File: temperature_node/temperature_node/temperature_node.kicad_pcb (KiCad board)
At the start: 4 copper layers, 23 x 24.5 mm, 35 parts, among them CN1 UART, J1 USB_C_Receptacle_USB2.0_16P, J2 S2B-PH-K-S, J3 IO9, U1 SHT40-AD1B-R3, U2 MCP73831-2-OT, U3 MIC5504-3.3YM5, U4 ESP32-C3-WROOM-02, U6 USBLC6-2P6

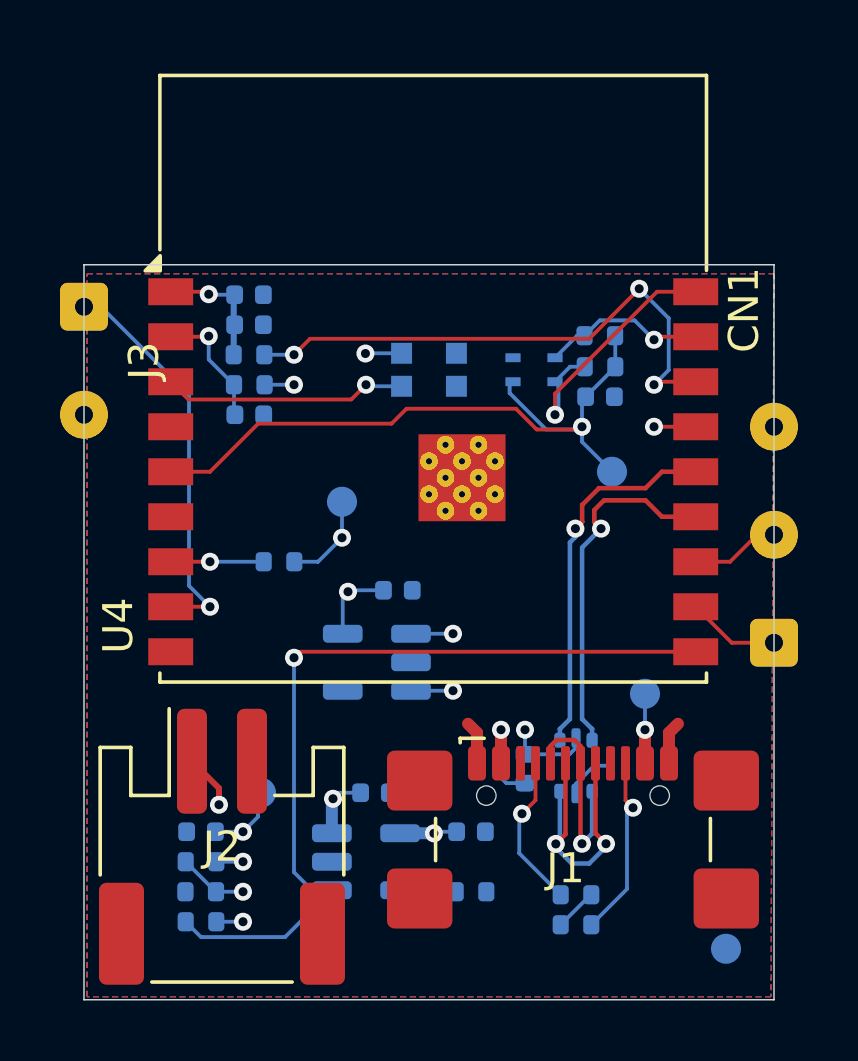
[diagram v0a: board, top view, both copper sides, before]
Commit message: Remove some DRC warnings
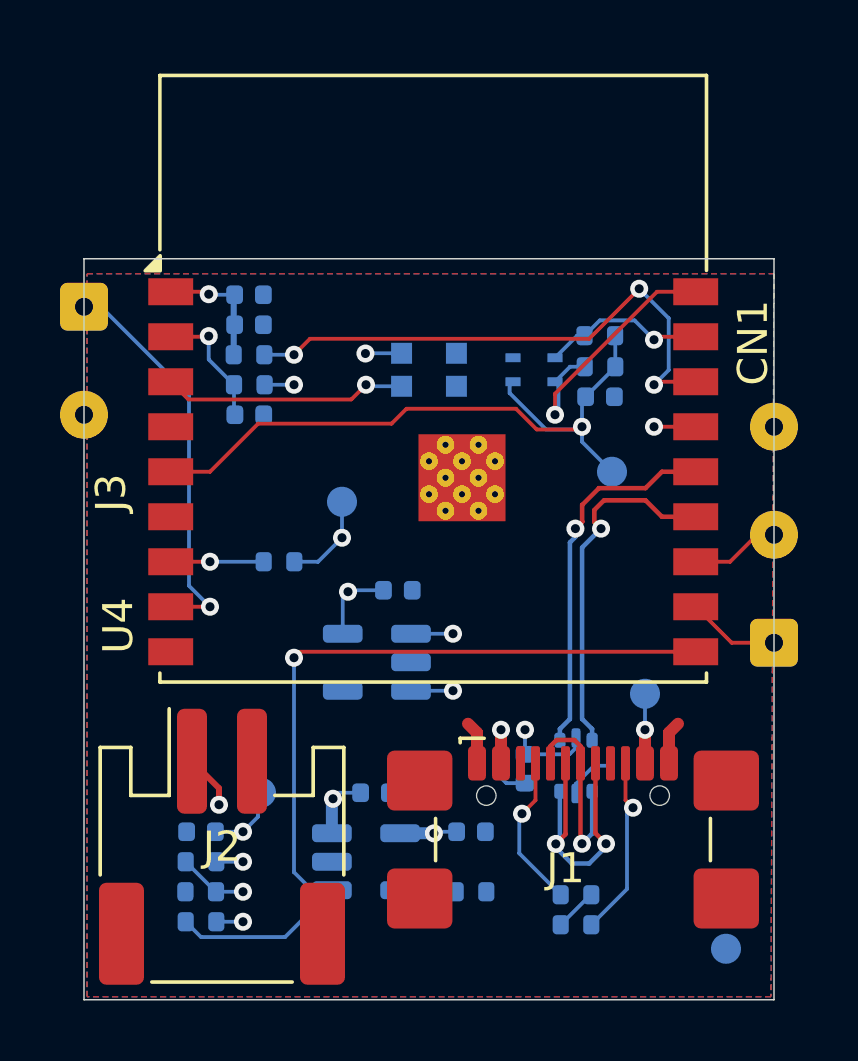
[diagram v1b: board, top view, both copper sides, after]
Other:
- board size 23 x 24.5 mm -> 23 x 24.7 mm
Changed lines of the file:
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@@
 		(tags "connector wire 0.1sqmm")
 		(property "Reference" "J3"
-			(at 1.8 -2 90)
+			(at 6.2 -0.9 90)
 			(layer "F.SilkS")
 			(effects
@@
 		)
 		(fp_text user "${REFERENCE}"
-			(at 1.8 0 360)
+			(at 1.8 0 0)
 			(layer "F.Fab")
 			(effects
@@
 		(tags "connector wire 0.1sqmm")
 		(property "Reference" "CN1"
-			(at 11.09 -1 90)
+			(at 10 -0.7 90)
 			(layer "F.SilkS")
 			(effects
@@
 		(tags "resistor")
 		(property "Reference" "R3"
-			(at 0 1.17 360)
+			(at 0 1.17 0)
 			(layer "B.SilkS")
 			(effects
@@
 		)
 		(property "Value" "10k"
-			(at 0 -1.17 360)
+			(at 0 -1.17 0)
 			(layer "B.Fab")
 			(effects
@@
 		)
 		(fp_text user "${REFERENCE}"
-			(at 0 0 360)
+			(at 0 0 0)
 			(layer "B.Fab")
 			(effects
@@
 		(tags "resistor")
 		(property "Reference" "R11"
-			(at 2.5 0 360)
+			(at 2.5 0 0)
 			(layer "B.SilkS")
 			(effects
@@
 		)
 		(property "Value" "100k"
-			(at 0 -1.17 360)
+			(at 0 -1.17 0)
 			(layer "B.Fab")
 			(effects
@@
 		)
 		(fp_text user "${REFERENCE}"
-			(at 0 0 360)
+			(at 0 0 0)
 			(layer "B.Fab")
 			(effects
@@
 		(tags "SOT TO_SOT_SMD")
 		(property "Reference" "U2"
-			(at 0 2.4 360)
+			(at 0 2.4 0)
 			(layer "B.SilkS")
 			(effects
@@
 		)
 		(property "Value" "MCP73831-2-OT"
-			(at 0 -2.4 360)
+			(at 0 -2.4 0)
 			(layer "B.Fab")
 			(effects
@@
 		)
 		(fp_text user "${REFERENCE}"
-			(at 0 0 360)
+			(at 0 0 0)
 			(layer "B.Fab")
 			(effects
@@
 		(tags "capacitor")
 		(property "Reference" "C2"
-			(at 2.5 0.5 360)
+			(at 2.5 0.5 0)
 			(layer "B.SilkS")
 			(effects
@@
 		)
 		(property "Value" "4u7"
-			(at 0 -1 360)
+			(at 0 -1 0)
 			(layer "B.Fab")
 			(effects
@@
 		)
 		(fp_text user "${REFERENCE}"
-			(at 0 0 360)
+			(at 0 0 0)
 			(layer "B.Fab")
 			(effects
@@
 		(tags "capacitor")
 		(property "Reference" "C5"
-			(at -0.049122 1.202403 360)
+			(at -0.049122 1.202403 0)
 			(layer "B.SilkS")
 			(effects
@@
 		)
 		(property "Value" "1u"
-			(at 0 -1.16 360)
+			(at 0 -1.16 0)
 			(layer "B.Fab")
 			(effects
@@
 		)
 		(fp_text user "${REFERENCE}"
-			(at 0 0 360)
+			(at 0 0 0)
 			(layer "B.Fab")
 			(effects
@@
 		(tags "resistor")
 		(property "Reference" "R12"
-			(at 2.49 -0.5 360)
+			(at 2.49 -0.5 0)
 			(layer "B.SilkS")
 			(effects
@@
 		)
 		(property "Value" "100k"
-			(at 0 -1.17 360)
+			(at 0 -1.17 0)
 			(layer "B.Fab")
 			(effects
@@
 		)
 		(fp_text user "${REFERENCE}"
-			(at 0 0 360)
+			(at 0 0 0)
 			(layer "B.Fab")
 			(effects
@@
 		)
 		(fp_text user "${REFERENCE}"
-			(at 0 0 360)
+			(at 0 0 0)
 			(layer "B.Fab")
 			(effects
@@
 		(tags "capacitor")
 		(property "Reference" "C3"
-			(at 3 0.5 360)
+			(at 3 0.5 0)
 			(layer "B.SilkS")
 			(effects
@@
 		)
 		(property "Value" "4u7"
-			(at 0 -1.5 360)
+			(at 0 -1.5 0)
 			(layer "B.Fab")
 			(effects
@@
 		)
 		(fp_text user "${REFERENCE}"
-			(at 0 0 360)
+			(at 0 0 0)
 			(layer "B.Fab")
 			(effects
@@
 		)
 		(property "Value" "1u"
-			(at 0 -1.16 360)
+			(at 0 -1.16 0)
 			(layer "B.Fab")
 			(effects
@@
 		)
 		(fp_text user "${REFERENCE}"
-			(at 0 0 360)
+			(at 0 0 0)
 			(layer "B.Fab")
 			(effects
@@
 		(tags "resistor")
 		(property "Reference" "R4"
-			(at 2 0 360)
+			(at 2 0 0)
 			(layer "B.SilkS")
 			(effects
@@
 		)
 		(property "Value" "10k"
-			(at 0 -1.17 360)
+			(at 0 -1.17 0)
 			(layer "B.Fab")
 			(effects
@@
 		)
 		(fp_text user "${REFERENCE}"
-			(at 0 0 360)
+			(at 0 0 0)
 			(layer "B.Fab")
 			(effects
@@
 	)
 	(gr_rect
-		(start 121 80)
+		(start 121 79.8)
 		(end 144 104.5)
 		(stroke

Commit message: Constellation pads added property for DRC
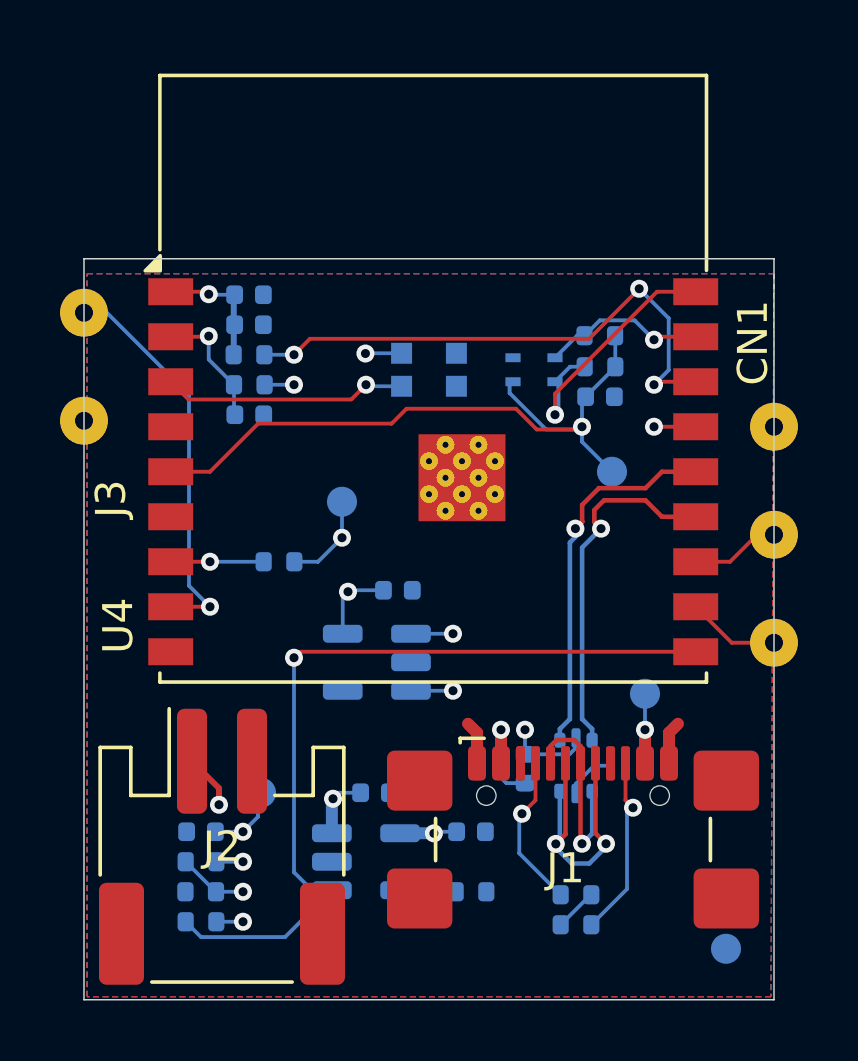
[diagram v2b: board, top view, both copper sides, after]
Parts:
- moved J3 0.20 mm to (121.0, 81.6)
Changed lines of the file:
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@@
 	(footprint "Connector_Wire:SolderWire-0.1sqmm_1x02_P3.6mm_D0.4mm_OD1mm"
 		(layer "F.Cu")
-		(at 121 81.4 -90)
+		(at 121 81.6 -90)
 		(descr "Soldered wire connection, for 2 times 0.1 mm² wires, basic insulation, conductor diameter 0.4mm, outer diameter 1mm, size source Multi-Contact FLEXI-E 0.1 (https://ec.staubli.com/AcroFiles/Catalogues/TM_Cab-Main-11014119_(en)_hi.pdf), bend radius 3 times outer diameter, generated with kicad-footprint-generator")
 		(tags "connector wire 0.1sqmm")
@@
 			)
 		)
-		(pad "1" thru_hole roundrect
+		(pad "1" thru_hole circle
 			(at 0 0 270)
 			(size 1.6 1.6)
 			(drill 0.6)
+			(property pad_prop_castellated)
 			(layers "*.Cu" "*.Mask")
 			(remove_unused_layers no)
-			(roundrect_rratio 0.15625)
 			(net 20 "Net-(J3-Pin_1)")
 			(pinfunction "Pin_1")
@@
 			(size 1.6 1.6)
 			(drill 0.6)
+			(property pad_prop_castellated)
 			(layers "*.Cu" "*.Mask")
 			(remove_unused_layers no)
@@
 			)
 		)
-		(pad "1" thru_hole roundrect
+		(pad "1" thru_hole circle
 			(at 0 0 90)
 			(size 1.6 1.6)
 			(drill 0.6)
+			(property pad_prop_castellated)
 			(layers "*.Cu" "*.Mask")
 			(remove_unused_layers no)
-			(roundrect_rratio 0.15625)
 			(net 8 "/RX")
 			(pinfunction "Pin_1")
@@
 			(size 1.6 1.6)
 			(drill 0.6)
+			(property pad_prop_castellated)
 			(layers "*.Cu" "*.Mask")
 			(remove_unused_layers no)
@@
 			(size 1.6 1.6)
 			(drill 0.6)
+			(property pad_prop_castellated)
 			(layers "*.Cu" "*.Mask")
 			(remove_unused_layers no)

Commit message: Apply sch changes
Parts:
- removed CN1: UART, Connector_Wire:SolderWire-0.1sqmm_1x03_P3.6mm_D0.4mm_OD1mm
- removed J3: IO9, Connector_Wire:SolderWire-0.1sqmm_1x02_P3.6mm_D0.4mm_OD1mm
- added TP6: RX, TestPoint:TestPoint_Pad_D1.0mm, B.Cu at (141.9, 88.0)
- added TP7: TX, TestPoint:TestPoint_Pad_D1.0mm, B.Cu at (141.9, 91.0)
- added TP8: IO9, TestPoint:TestPoint_Pad_D1.0mm, B.Cu at (141.9, 94.1)
- moved TP1 3.64 mm to (141.9, 97.2)
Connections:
- U4 pad 8: Net-(J3-Pin_1) -> /IO9
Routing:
- net /IO9: track 0.00 -> 19.1 mm, vias 0 -> 1
- net Net-(J3-Pin_1): track 12.8 -> 0.00 mm, vias 1 -> 0
- net /RX: track 2.54 -> 9.70 mm, vias 0 -> 1
- net /TX: track 2.42 -> 6.59 mm, vias 0 -> 1
- net VBUS: track 8.28 -> 9.99 mm

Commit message: PCB DRC Ok
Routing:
- net GND: track 7.01 -> 23.9 mm, vias 0 -> 23
- net /RX: track 9.70 -> 7.15 mm
- net /TX: track 6.59 -> 4.17 mm
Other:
- board size 23 x 24.7 mm -> 23 x 31.3 mm

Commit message: Reanotate PCB and SCH
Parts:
- renumbered C6 to C2, C8 to C3, C7 to C4, C3 to C6, C4 to C7, C9 to C8, C2 to C9, D3 to D1, R2 to R1, R4 to R10, R9 to R11, R10 to R2, R8 to R3, R1 to R4, R3 to R5, R5 to R6, R11 to R7, R12 to R8, R6 to R9, TP6 to TP1, TP4 to TP2, TP7 to TP4, TP1 to TP6, TP8 to TP7, TP2 to TP8, U4 to U1, U1 to U2, U2 to U3, U6 to U4, U3 to U5
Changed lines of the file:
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@@
 		(descr "RF Module, ESP32-C3 WROOM-02, Wi-Fi and Bluetooth, BLE, onboard antenna, https://www.espressif.com/sites/default/files/documentation/esp32-c3-wroom-02_datasheet_en.pdf")
 		(tags "ESP32-C3 WROOM-02 espressif")
-		(property "Reference" "U4"
+		(property "Reference" "U1"
 			(at -10.5 5.13 90)
 			(layer "F.SilkS")
@@
 		(descr "Resistor SMD 0402 (1005 Metric), square (rectangular) end terminal, IPC_7351 nominal, (Body size source: IPC-SM-782 page 72, https://www.pcb-3d.com/wordpress/wp-content/uploads/ipc-sm-782a_amendment_1_and_2.pdf), generated with kicad-footprint-generator")
 		(tags "resistor")
-		(property "Reference" "R3"
+		(property "Reference" "R5"
 			(at 0 1.17 0)
 			(layer "B.SilkS")
@@
 		(descr "Resistor SMD 0402 (1005 Metric), square (rectangular) end terminal, IPC_7351 nominal, (Body size source: IPC-SM-782 page 72, https://www.pcb-3d.com/wordpress/wp-content/uploads/ipc-sm-782a_amendment_1_and_2.pdf), generated with kicad-footprint-generator")
 		(tags "resistor")
-		(property "Reference" "R5"
+		(property "Reference" "R6"
 			(at -2.5 0 0)
 			(layer "B.SilkS")
@@
 		(descr "Sensirion, SHT40, SHT41, SHT45, DFN, 4 Pin (https://sensirion.com/media/documents/33FD6951/624C4357/Datasheet_SHT4x.pdf)")
 		(tags "DFN NoLead")
-		(property "Reference" "U1"
+		(property "Reference" "U2"
 			(at 0.2 -2 0)
 			(layer "B.SilkS")
@@
 		(descr "Resistor SMD 0402 (1005 Metric), square (rectangular) end terminal, IPC_7351 nominal, (Body size source: IPC-SM-782 page 72, https://www.pcb-3d.com/wordpress/wp-content/uploads/ipc-sm-782a_amendment_1_and_2.pdf), generated with kicad-footprint-generator")
 		(tags "resistor")
-		(property "Reference" "R11"
+		(property "Reference" "R7"
 			(at 2.5 0 0)
 			(layer "B.SilkS")
@@
 		(descr "Capacitor SMD 0402 (1005 Metric), square (rectangular) end terminal, IPC_7351 nominal, (Body size source: IPC-SM-782 page 76, https://www.pcb-3d.com/wordpress/wp-content/uploads/ipc-sm-782a_amendment_1_and_2.pdf), generated with kicad-footprint-generator")
 		(tags "capacitor")
-		(property "Reference" "C7"
+		(property "Reference" "C4"
 			(at -2.5 0 0)
 			(layer "B.SilkS")
@@
 		(descr "Resistor SMD 0402 (1005 Metric), square (rectangular) end terminal, IPC_7351 nominal, (Body size source: IPC-SM-782 page 72, https://www.pcb-3d.com/wordpress/wp-content/uploads/ipc-sm-782a_amendment_1_and_2.pdf), generated with kicad-footprint-generator")
 		(tags "resistor")
-		(property "Reference" "R8"
+		(property "Reference" "R3"
 			(at -2.298321 -1.073385 0)
 			(layer "B.SilkS")
@@
 		(descr "SMD pad as test Point, diameter 1.0mm")
 		(tags "test point SMD pad")
-		(property "Reference" "TP1"
+		(property "Reference" "TP6"
 			(at 0 -1.9 0)
 			(layer "B.SilkS")
@@
 		(descr "SMD pad as test Point, diameter 1.0mm")
 		(tags "test point SMD pad")
-		(property "Reference" "TP6"
+		(property "Reference" "TP1"
 			(at 0 1.448 0)
 			(layer "B.SilkS")
@@
 		(descr "SOT, 5 Pin (https://www.jedec.org/sites/default/files/docs/Mo-178c.PDF variant AA), generated with kicad-footprint-generator ipc_gullwing_generator.py")
 		(tags "SOT TO_SOT_SMD")
-		(property "Reference" "U2"
+		(property "Reference" "U3"
 			(at 0 2.4 0)
 			(layer "B.SilkS")
@@
 		(descr "SMD pad as test Point, diameter 1.0mm")
 		(tags "test point SMD pad")
-		(property "Reference" "TP2"
+		(property "Reference" "TP8"
 			(at 2.5 0 0)
 			(layer "B.SilkS")
@@
 		(descr "Capacitor SMD 0402 (1005 Metric), square (rectangular) end terminal, IPC_7351 nominal, (Body size source: IPC-SM-782 page 76, https://www.pcb-3d.com/wordpress/wp-content/uploads/ipc-sm-782a_amendment_1_and_2.pdf), generated with kicad-footprint-generator")
 		(tags "capacitor")
-		(property "Reference" "C6"
+		(property "Reference" "C2"
 			(at -2.5 1.5 0)
 			(layer "B.SilkS")
@@
 		(descr "Capacitor SMD 0402 (1005 Metric), square (rectangular) end terminal, IPC_7351 nominal, (Body size source: IPC-SM-782 page 76, https://www.pcb-3d.com/wordpress/wp-content/uploads/ipc-sm-782a_amendment_1_and_2.pdf), generated with kicad-footprint-generator")
 		(tags "capacitor")
-		(property "Reference" "C8"
+		(property "Reference" "C3"
 			(at -2.5 0.5 0)
 			(layer "B.SilkS")
@@
 		(descr "Resistor SMD 0402 (1005 Metric), square (rectangular) end terminal, IPC_7351 nominal, (Body size source: IPC-SM-782 page 72, https://www.pcb-3d.com/wordpress/wp-content/uploads/ipc-sm-782a_amendment_1_and_2.pdf), generated with kicad-footprint-generator")
 		(tags "resistor")
-		(property "Reference" "R2"
+		(property "Reference" "R1"
 			(at -2.307825 0.365343 0)
 			(layer "B.SilkS")
@@
 		(descr "SMD pad as test Point, diameter 1.0mm")
 		(tags "test point SMD pad")
-		(property "Reference" "TP7"
+		(property "Reference" "TP4"
 			(at 0 1.448 0)
 			(layer "B.SilkS")
@@
 		(descr "Resistor SMD 0402 (1005 Metric), square (rectangular) end terminal, IPC_7351 nominal, (Body size source: IPC-SM-782 page 72, https://www.pcb-3d.com/wordpress/wp-content/uploads/ipc-sm-782a_amendment_1_and_2.pdf), generated with kicad-footprint-generator")
 		(tags "resistor")
-		(property "Reference" "R6"
+		(property "Reference" "R9"
 			(at 0 1.2 0)
 			(layer "B.SilkS")
@@
 		(descr "SMD pad as test Point, diameter 1.0mm")
 		(tags "test point SMD pad")
-		(property "Reference" "TP4"
+		(property "Reference" "TP2"
 			(at 2.5 0 0)
 			(layer "B.SilkS")
@@
 		(descr "Capacitor SMD 0402 (1005 Metric), square (rectangular) end terminal, IPC_7351 nominal, (Body size source: IPC-SM-782 page 76, https://www.pcb-3d.com/wordpress/wp-content/uploads/ipc-sm-782a_amendment_1_and_2.pdf), generated with kicad-footprint-generator")
 		(tags "capacitor")
-		(property "Reference" "C9"
+		(property "Reference" "C8"
 			(at -0.6 1.16 90)
 			(layer "B.SilkS")
@@
 		(descr "Capacitor SMD 0402 (1005 Metric), square (rectangular) end terminal, IPC_7351 nominal, (Body size source: IPC-SM-782 page 76, https://www.pcb-3d.com/wordpress/wp-content/uploads/ipc-sm-782a_amendment_1_and_2.pdf), generated with kicad-footprint-generator")
 		(tags "capacitor")
-		(property "Reference" "C2"
+		(property "Reference" "C9"
 			(at 2.5 0.5 0)
 			(layer "B.SilkS")
@@
 		(descr "Resistor SMD 0402 (1005 Metric), square (rectangular) end terminal, IPC_7351 nominal, (Body size source: IPC-SM-782 page 72, https://www.pcb-3d.com/wordpress/wp-content/uploads/ipc-sm-782a_amendment_1_and_2.pdf), generated with kicad-footprint-generator")
 		(tags "resistor")
-		(property "Reference" "R12"
+		(property "Reference" "R8"
 			(at 2.49 -0.4 0)
 			(layer "B.SilkS")
@@
 		(descr "SOT666")
 		(tags "SOT-666")
-		(property "Reference" "U6"
+		(property "Reference" "U4"
 			(at 2.4 0 180)
 			(layer "B.SilkS")
@@
 		(descr "Capacitor SMD 0402 (1005 Metric), square (rectangular) end terminal, IPC_7351 nominal, (Body size source: IPC-SM-782 page 76, https://www.pcb-3d.com/wordpress/wp-content/uploads/ipc-sm-782a_amendment_1_and_2.pdf), generated with kicad-footprint-generator")
 		(tags "capacitor")
-		(property "Reference" "C3"
+		(property "Reference" "C6"
 			(at 3 0.5 0)
 			(layer "B.SilkS")
@@
 		(descr "Capacitor SMD 0402 (1005 Metric), square (rectangular) end terminal, IPC_7351 nominal, (Body size source: IPC-SM-782 page 76, https://www.pcb-3d.com/wordpress/wp-content/uploads/ipc-sm-782a_amendment_1_and_2.pdf), generated with kicad-footprint-generator")
 		(tags "capacitor")
-		(property "Reference" "C4"
+		(property "Reference" "C7"
 			(at 2 0 90)
 			(layer "B.SilkS")
@@
 		(descr "Resistor SMD 0402 (1005 Metric), square (rectangular) end terminal, IPC_7351 nominal, (Body size source: IPC-SM-782 page 72, https://www.pcb-3d.com/wordpress/wp-content/uploads/ipc-sm-782a_amendment_1_and_2.pdf), generated with kicad-footprint-generator")
 		(tags "resistor")
-		(property "Reference" "R1"
+		(property "Reference" "R4"
 			(at -2.3 -0.1 0)
 			(layer "B.SilkS")
@@
 		(descr "SOT, 5 Pin (https://www.jedec.org/sites/default/files/docs/Mo-178c.PDF variant AA), generated with kicad-footprint-generator ipc_gullwing_generator.py")
 		(tags "SOT TO_SOT_SMD")
-		(property "Reference" "U3"
+		(property "Reference" "U5"
 			(at 3.1375 -2.05 0)
 			(layer "B.SilkS")
@@
 		(descr "Resistor SMD 0402 (1005 Metric), square (rectangular) end terminal, IPC_7351 nominal, (Body size source: IPC-SM-782 page 72, https://www.pcb-3d.com/wordpress/wp-content/uploads/ipc-sm-782a_amendment_1_and_2.pdf), generated with kicad-footprint-generator")
 		(tags "resistor")
-		(property "Reference" "R4"
+		(property "Reference" "R10"
 			(at 2 -0.8 0)
 			(layer "B.SilkS")
@@
 		(descr "SMD pad as test Point, diameter 1.0mm")
 		(tags "test point SMD pad")
-		(property "Reference" "TP8"
+		(property "Reference" "TP7"
 			(at 0 1.448 0)
 			(layer "B.SilkS")
@@
 		(descr "Resistor SMD 0402 (1005 Metric), square (rectangular) end terminal, IPC_7351 nominal, (Body size source: IPC-SM-782 page 72, https://www.pcb-3d.com/wordpress/wp-content/uploads/ipc-sm-782a_amendment_1_and_2.pdf), generated with kicad-footprint-generator")
 		(tags "resistor")
-		(property "Reference" "R9"
+		(property "Reference" "R11"
 			(at -2.5 0 0)
 			(layer "B.SilkS")
@@
 		(descr "2.0mm x 2.0mm Addressable RGB LED NeoPixel Nano, 12 mA, https://cdn-shop.adafruit.com/product-files/4684/4684_WS2812B-2020_V1.3_EN.pdf")
 		(tags "LED RGB NeoPixel Nano PLCC-4 2020")
-		(property "Reference" "D3"
+		(property "Reference" "D1"
 			(at 0 2 0)
 			(layer "B.SilkS")
@@
 		(descr "Resistor SMD 0402 (1005 Metric), square (rectangular) end terminal, IPC_7351 nominal, (Body size source: IPC-SM-782 page 72, https://www.pcb-3d.com/wordpress/wp-content/uploads/ipc-sm-782a_amendment_1_and_2.pdf), generated with kicad-footprint-generator")
 		(tags "resistor")
-		(property "Reference" "R10"
+		(property "Reference" "R2"
 			(at 3 -1 0)
 			(layer "B.SilkS")
